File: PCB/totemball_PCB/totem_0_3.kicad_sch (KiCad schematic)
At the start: 84 parts, among them J1 MJ-4PP-9, J2 MJ-4PP-9, U1 xiao-ble, U2 xiao-ble

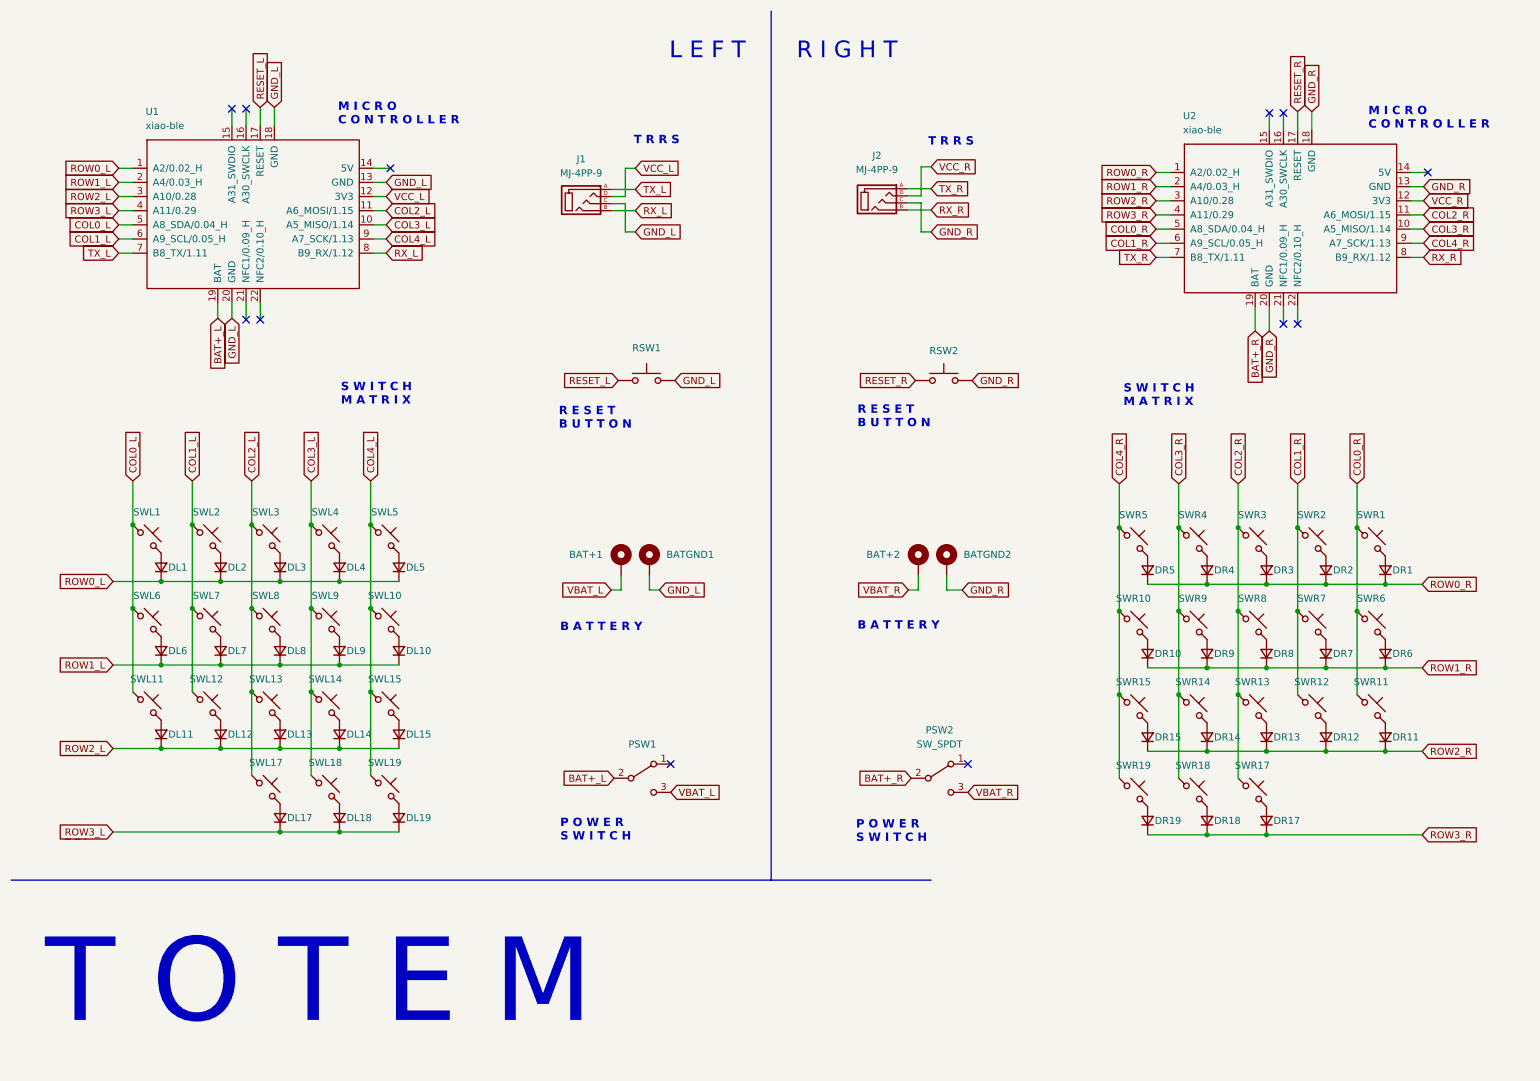
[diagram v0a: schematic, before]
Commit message: update schematic
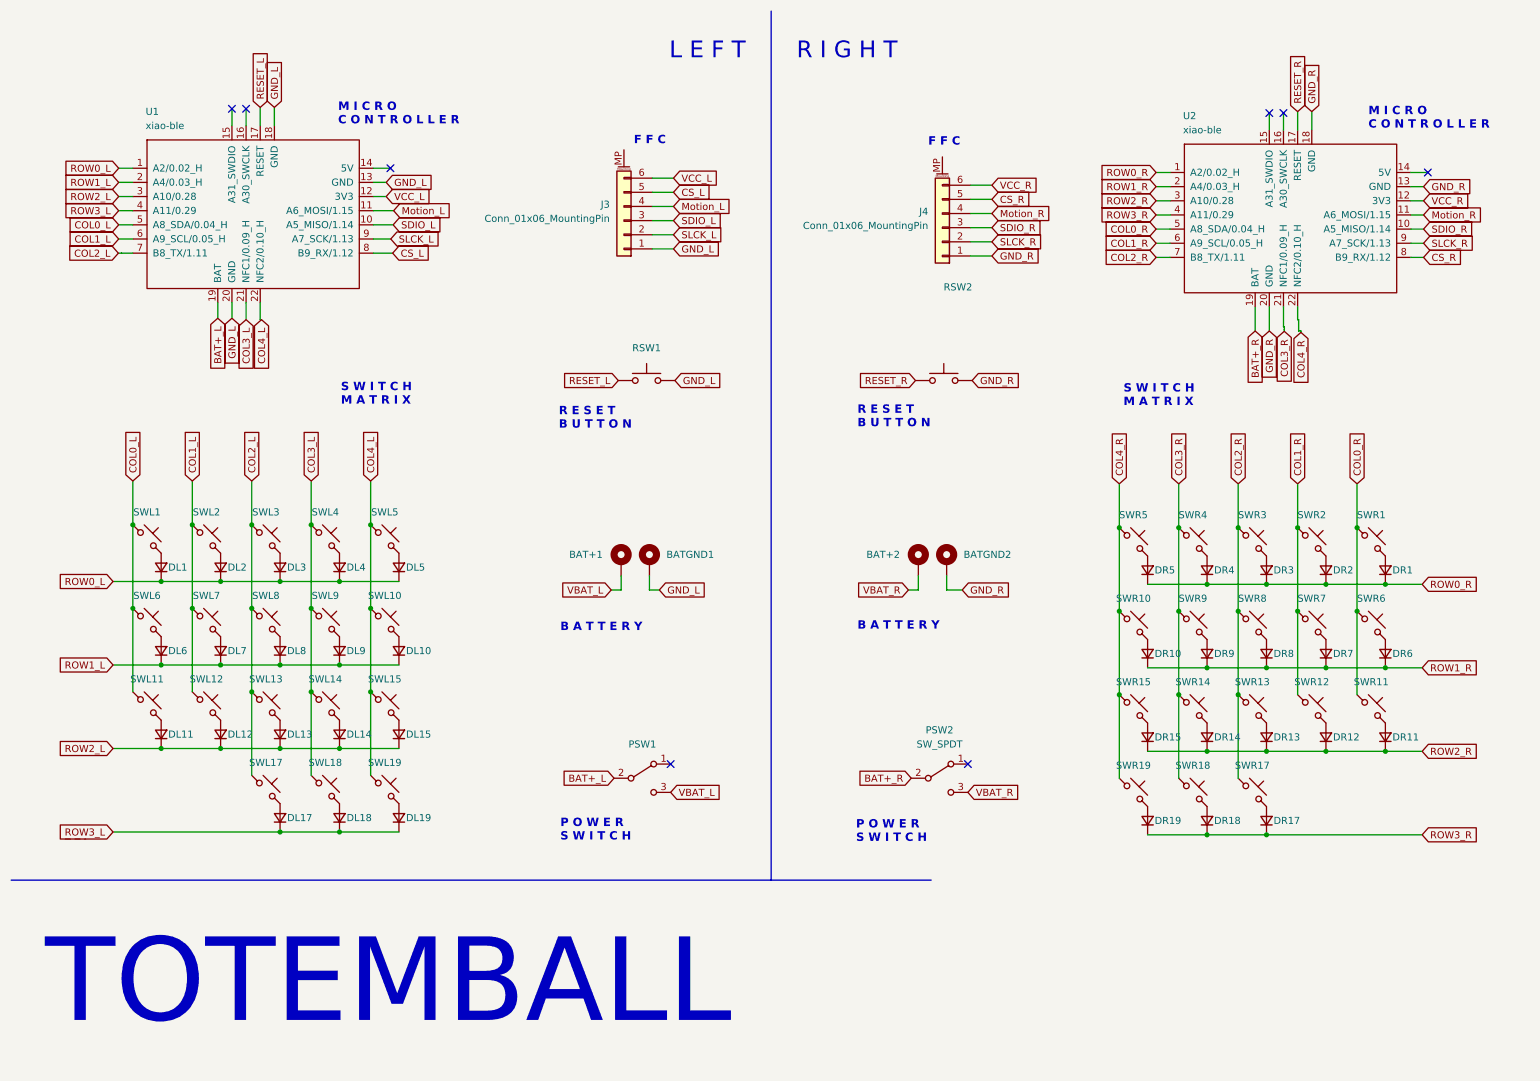
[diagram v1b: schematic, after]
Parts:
- removed J1, J2: MJ-4PP-9, TOTEMlib:MJ-4PP-9_1side, symbol kbd:MJ-4PP-9
- added J3, J4: Conn_01x06_MountingPin, TOTEMlib:GT-F0501SR10-06S1101, symbol Connector_Generic_MountingPin:Conn_01x06_MountingPin
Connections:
- net TX_L is gone; now on net COL2_L: U1.7 (B8_TX/1.11)
- net TX_R is gone; now on net COL2_R: U2.7 (B8_TX/1.11)
- net COL2_L: no longer U1.11 (A6_MOSI/1.15)
- net COL2_R: no longer U2.11 (A6_MOSI/1.15)
- net COL3_L: now also U1.21 (NFC1/0.09_H); no longer U1.10 (A5_MISO/1.14)
- net COL3_R: now also U2.21 (NFC1/0.09_H); no longer U2.10 (A5_MISO/1.14)
- net COL4_L: now also U1.22 (NFC2/0.10_H); no longer U1.9 (A7_SCK/1.13)
- net COL4_R: now also U2.22 (NFC2/0.10_H); no longer U2.9 (A7_SCK/1.13)
- net GND_L: now also J3.1 (Pin_1)
- net GND_R: now also J4.1 (Pin_1)
- net VCC_L: now also J3.6 (Pin_6)
- net VCC_R: now also J4.6 (Pin_6)
- net RX_L renamed CS_L
- net CS_L: now also J3.5 (Pin_5)
- net RX_R renamed CS_R
- net CS_R: now also J4.5 (Pin_5)
- new net Motion_L: J3.4 (Pin_4), U1.11 (A6_MOSI/1.15)
- new net Motion_R: J4.4 (Pin_4), U2.11 (A6_MOSI/1.15)
- new net SDIO_L: J3.3 (Pin_3), U1.10 (A5_MISO/1.14)
- new net SDIO_R: J4.3 (Pin_3), U2.10 (A5_MISO/1.14)
- new net SLCK_L: J3.2 (Pin_2), U1.9 (A7_SCK/1.13)
- new net SLCK_R: J4.2 (Pin_2), U2.9 (A7_SCK/1.13)
- no-connect marks 12 -> 8
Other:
- note added: "F F C"
- note added: "TOTEMBALL"
- note removed: "T O T E M"
- note removed: "T R R S"
- title: TOTEM split keyboard -> TOTEMBALL split keyboard

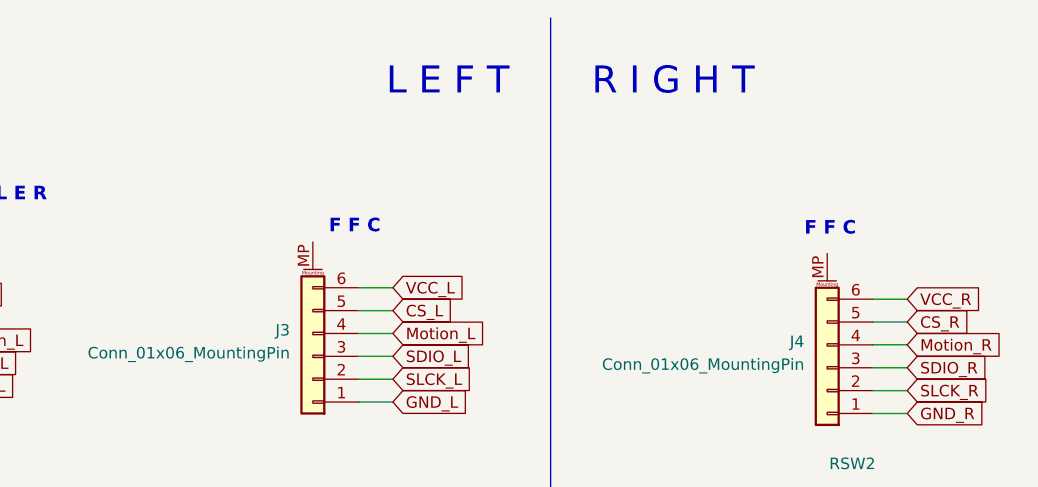
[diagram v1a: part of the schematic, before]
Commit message: wired right ffc connector
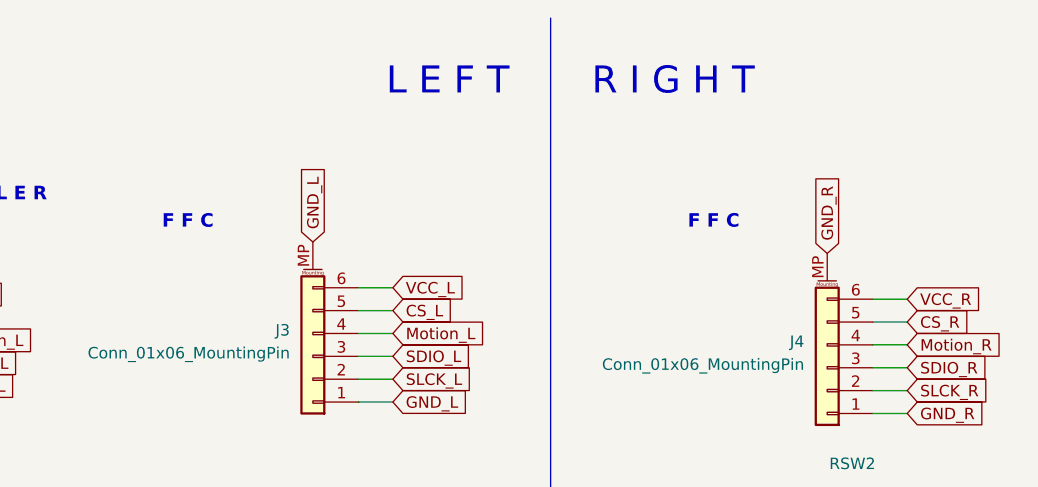
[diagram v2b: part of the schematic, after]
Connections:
- net GND_L: now also J3.MP (MountPin)
- net GND_R: now also J4.MP (MountPin)
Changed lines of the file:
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@@
 	(text "F F C"
 		(exclude_from_sim no)
-		(at 176.53 36.322 0)
+		(at 163.576 35.56 0)
 		(effects
 			(font
@@
 	(text "F F C"
 		(exclude_from_sim no)
-		(at 123.698 36.068 0)
+		(at 105.156 35.56 0)
 		(effects
 			(font
@@
 		)
 	)
+	(global_label "GND_R"
+		(shape input)
+		(at 179.07 38.1 90)
+		(fields_autoplaced yes)
+		(effects
+			(font
+				(size 1.27 1.27)
+			)
+			(justify left)
+		)
+		(property "Intersheetrefs" "${INTERSHEET_REFS}"
+			(at 179.07 29.0067 90)
+			(effects
+				(font
+					(size 1.27 1.27)
+				)
+				(justify left)
+				(hide yes)
+			)
+		)
+	)
 	(global_label "ROW0_R"
 		(shape input)
@@
 		)
 	)
+	(global_label "GND_L"
+		(shape input)
+		(at 121.92 36.83 90)
+		(fields_autoplaced yes)
+		(effects
+			(font
+				(size 1.27 1.27)
+			)
+			(justify left)
+		)
+		(property "Intersheetrefs" "${INTERSHEET_REFS}"
+			(at 121.92 27.9786 90)
+			(effects
+				(font
+					(size 1.27 1.27)
+				)
+				(justify left)
+				(hide yes)
+			)
+		)
+	)
 	(global_label "SDIO_R"
 		(shape input)
@@
 		)
 		(property "Intersheetrefs" "${INTERSHEET_REFS}"
-			(at 139.0893 54.5306 0)
-			(effects
-				(font
+			(at 139.6614 54.61 0)
+			(effects
+				(font

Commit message: socket now supports both v1 and v2 hotswap
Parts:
- SWL1, SWL10, SWL11, SWL12, SWL13, SWL14, SWL15, SWL17, SWL18, SWL19, SWL2, SWL3, SWL4, SWL5, SWL6, SWL7, SWL8, SWL9, SWR1, SWR10, SWR11, SWR12, SWR13, SWR14, SWR15, SWR17, SWR18, SWR19, SWR2, SWR3, SWR4, SWR5, SWR6, SWR7, SWR8, SWR9: footprint TOTEMlib:Kailh_socket_PG1350_optional -> TOTEMlib:SW_Kailh_Choc_V1V2_HotSwap_Hybrid
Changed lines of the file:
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@@
 			)
 		)
-		(property "Footprint" "TOTEMlib:Kailh_socket_PG1350_optional"
+		(property "Footprint" "TOTEMlib:SW_Kailh_Choc_V1V2_HotSwap_Hybrid"
 			(at 245.364 107.188 0)
 			(effects
@@
 			)
 		)
-		(property "Footprint" "TOTEMlib:Kailh_socket_PG1350_optional"
+		(property "Footprint" "TOTEMlib:SW_Kailh_Choc_V1V2_HotSwap_Hybrid"
 			(at 57.658 151.638 0)
 			(effects
@@
 			)
 		)
-		(property "Footprint" "TOTEMlib:Kailh_socket_PG1350_optional"
+		(property "Footprint" "TOTEMlib:SW_Kailh_Choc_V1V2_HotSwap_Hybrid"
 			(at 68.326 106.68 0)
 			(effects
@@
 			)
 		)
-		(property "Footprint" "TOTEMlib:Kailh_socket_PG1350_optional"
+		(property "Footprint" "TOTEMlib:SW_Kailh_Choc_V1V2_HotSwap_Hybrid"
 			(at 234.696 107.188 0)
 			(effects
@@
 			)
 		)
-		(property "Footprint" "TOTEMlib:Kailh_socket_PG1350_optional"
+		(property "Footprint" "TOTEMlib:SW_Kailh_Choc_V1V2_HotSwap_Hybrid"
 			(at 57.658 106.68 0)
 			(effects
@@
 			)
 		)
-		(property "Footprint" "TOTEMlib:Kailh_socket_PG1350_optional"
+		(property "Footprint" "TOTEMlib:SW_Kailh_Choc_V1V2_HotSwap_Hybrid"
 			(at 213.36 122.174 0)
 			(effects
@@
 			)
 		)
-		(property "Footprint" "TOTEMlib:Kailh_socket_PG1350_optional"
+		(property "Footprint" "TOTEMlib:SW_Kailh_Choc_V1V2_HotSwap_Hybrid"
 			(at 245.364 137.16 0)
 			(effects
@@
 			)
 		)
-		(property "Footprint" "TOTEMlib:Kailh_socket_PG1350_optional"
+		(property "Footprint" "TOTEMlib:SW_Kailh_Choc_V1V2_HotSwap_Hybrid"
 			(at 234.696 122.174 0)
 			(effects
@@
 			)
 		)
-		(property "Footprint" "TOTEMlib:Kailh_socket_PG1350_optional"
+		(property "Footprint" "TOTEMlib:SW_Kailh_Choc_V1V2_HotSwap_Hybrid"
 			(at 46.99 121.666 0)
 			(effects
@@
 			)
 		)
-		(property "Footprint" "TOTEMlib:Kailh_socket_PG1350_optional"
+		(property "Footprint" "TOTEMlib:SW_Kailh_Choc_V1V2_HotSwap_Hybrid"
 			(at 234.696 137.16 0)
 			(effects
@@
 			)
 		)
-		(property "Footprint" "TOTEMlib:Kailh_socket_PG1350_optional"
+		(property "Footprint" "TOTEMlib:SW_Kailh_Choc_V1V2_HotSwap_Hybrid"
 			(at 213.36 107.188 0)
 			(effects
@@
 			)
 		)
-		(property "Footprint" "TOTEMlib:Kailh_socket_PG1350_optional"
+		(property "Footprint" "TOTEMlib:SW_Kailh_Choc_V1V2_HotSwap_Hybrid"
 			(at 57.658 121.666 0)
 			(effects
@@
 			)
 		)
-		(property "Footprint" "TOTEMlib:Kailh_socket_PG1350_optional"
+		(property "Footprint" "TOTEMlib:SW_Kailh_Choc_V1V2_HotSwap_Hybrid"
 			(at 68.326 136.652 0)
 			(effects
@@
 			)
 		)
-		(property "Footprint" "TOTEMlib:Kailh_socket_PG1350_optional"
+		(property "Footprint" "TOTEMlib:SW_Kailh_Choc_V1V2_HotSwap_Hybrid"
 			(at 78.994 151.638 0)
 			(effects
@@
 			)
 		)
-		(property "Footprint" "TOTEMlib:Kailh_socket_PG1350_optional"
+		(property "Footprint" "TOTEMlib:SW_Kailh_Choc_V1V2_HotSwap_Hybrid"
 			(at 213.36 152.146 0)
 			(effects
@@
 			)
 		)
-		(property "Footprint" "TOTEMlib:Kailh_socket_PG1350_optional"
+		(property "Footprint" "TOTEMlib:SW_Kailh_Choc_V1V2_HotSwap_Hybrid"
 			(at 234.696 152.146 0)
 			(effects
@@
 			)
 		)
-		(property "Footprint" "TOTEMlib:Kailh_socket_PG1350_optional"
+		(property "Footprint" "TOTEMlib:SW_Kailh_Choc_V1V2_HotSwap_Hybrid"
 			(at 245.364 122.174 0)
 			(effects
@@
 			)
 		)
-		(property "Footprint" "TOTEMlib:Kailh_socket_PG1350_optional"
+		(property "Footprint" "TOTEMlib:SW_Kailh_Choc_V1V2_HotSwap_Hybrid"
 			(at 36.322 106.68 0)
 			(effects
@@
 			)
 		)
-		(property "Footprint" "TOTEMlib:Kailh_socket_PG1350_optional"
+		(property "Footprint" "TOTEMlib:SW_Kailh_Choc_V1V2_HotSwap_Hybrid"
 			(at 68.326 121.666 0)
 			(effects
@@
 			)
 		)
-		(property "Footprint" "TOTEMlib:Kailh_socket_PG1350_optional"
+		(property "Footprint" "TOTEMlib:SW_Kailh_Choc_V1V2_HotSwap_Hybrid"
 			(at 78.994 106.68 0)
 			(effects
@@
 			)
 		)
-		(property "Footprint" "TOTEMlib:Kailh_socket_PG1350_optional"
+		(property "Footprint" "TOTEMlib:SW_Kailh_Choc_V1V2_HotSwap_Hybrid"
 			(at 224.028 137.16 0)
 			(effects
@@
 			)
 		)
-		(property "Footprint" "TOTEMlib:Kailh_socket_PG1350_optional"
+		(property "Footprint" "TOTEMlib:SW_Kailh_Choc_V1V2_HotSwap_Hybrid"
 			(at 46.99 106.68 0)
 			(effects
@@
 			)
 		)
-		(property "Footprint" "TOTEMlib:Kailh_socket_PG1350_optional"
+		(property "Footprint" "TOTEMlib:SW_Kailh_Choc_V1V2_HotSwap_Hybrid"
 			(at 78.994 136.652 0)
 			(effects
@@
 			)
 		)
-		(property "Footprint" "TOTEMlib:Kailh_socket_PG1350_optional"
+		(property "Footprint" "TOTEMlib:SW_Kailh_Choc_V1V2_HotSwap_Hybrid"
 			(at 78.994 121.666 0)
 			(effects
@@
 			)
 		)
-		(property "Footprint" "TOTEMlib:Kailh_socket_PG1350_optional"
+		(property "Footprint" "TOTEMlib:SW_Kailh_Choc_V1V2_HotSwap_Hybrid"
 			(at 213.36 137.16 0)
 			(effects
@@
 			)
 		)
-		(property "Footprint" "TOTEMlib:Kailh_socket_PG1350_optional"
+		(property "Footprint" "TOTEMlib:SW_Kailh_Choc_V1V2_HotSwap_Hybrid"
 			(at 57.658 136.652 0)
 			(effects
@@
 			)
 		)
-		(property "Footprint" "TOTEMlib:Kailh_socket_PG1350_optional"
+		(property "Footprint" "TOTEMlib:SW_Kailh_Choc_V1V2_HotSwap_Hybrid"
 			(at 256.032 107.188 0)
 			(effects
@@
 			)
 		)
-		(property "Footprint" "TOTEMlib:Kailh_socket_PG1350_optional"
+		(property "Footprint" "TOTEMlib:SW_Kailh_Choc_V1V2_HotSwap_Hybrid"
 			(at 224.028 122.174 0)
 			(effects
@@
 			)
 		)
-		(property "Footprint" "TOTEMlib:Kailh_socket_PG1350_optional"
+		(property "Footprint" "TOTEMlib:SW_Kailh_Choc_V1V2_HotSwap_Hybrid"
 			(at 256.032 122.174 0)
 			(effects
@@
 			)
 		)
-		(property "Footprint" "TOTEMlib:Kailh_socket_PG1350_optional"
+		(property "Footprint" "TOTEMlib:SW_Kailh_Choc_V1V2_HotSwap_Hybrid"
 			(at 46.99 136.652 0)
 			(effects
@@
 			)
 		)
-		(property "Footprint" "TOTEMlib:Kailh_socket_PG1350_optional"
+		(property "Footprint" "TOTEMlib:SW_Kailh_Choc_V1V2_HotSwap_Hybrid"
 			(at 68.326 151.638 0)
 			(effects
@@
 			)
 		)
-		(property "Footprint" "TOTEMlib:Kailh_socket_PG1350_optional"
+		(property "Footprint" "TOTEMlib:SW_Kailh_Choc_V1V2_HotSwap_Hybrid"
 			(at 36.322 121.666 0)
 			(effects
@@
 			)
 		)
-		(property "Footprint" "TOTEMlib:Kailh_socket_PG1350_optional"
+		(property "Footprint" "TOTEMlib:SW_Kailh_Choc_V1V2_HotSwap_Hybrid"
 			(at 224.028 107.188 0)
 			(effects
@@
 			)
 		)
-		(property "Footprint" "TOTEMlib:Kailh_socket_PG1350_optional"
+		(property "Footprint" "TOTEMlib:SW_Kailh_Choc_V1V2_HotSwap_Hybrid"
 			(at 224.028 152.146 0)
 			(effects
@@
 			)
 		)
-		(property "Footprint" "TOTEMlib:Kailh_socket_PG1350_optional"
+		(property "Footprint" "TOTEMlib:SW_Kailh_Choc_V1V2_HotSwap_Hybrid"
 			(at 36.322 136.652 0)
 			(effects
@@
 			)
 		)
-		(property "Footprint" "TOTEMlib:Kailh_socket_PG1350_optional"
+		(property "Footprint" "TOTEMlib:SW_Kailh_Choc_V1V2_HotSwap_Hybrid"
 			(at 256.032 137.16 0)
 			(effects
